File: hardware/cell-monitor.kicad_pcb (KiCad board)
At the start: 2 copper layers, 23 x 45 mm, 15 parts, among them J1 CELL, J2 COMM, J3 COMM, Q1 SI2312BDS, U1 ATTINY85, U2 ADuM1201AR

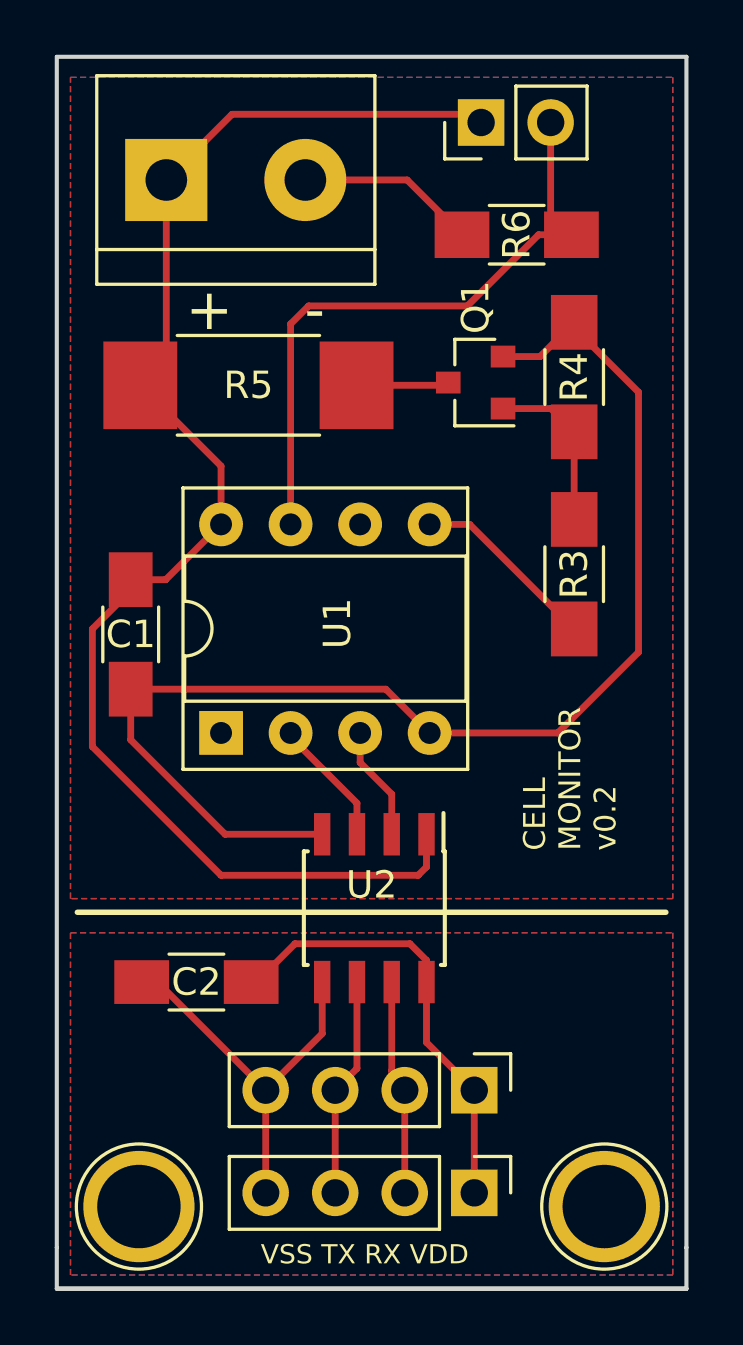
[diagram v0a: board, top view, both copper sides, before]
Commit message: Remove temp related hardware
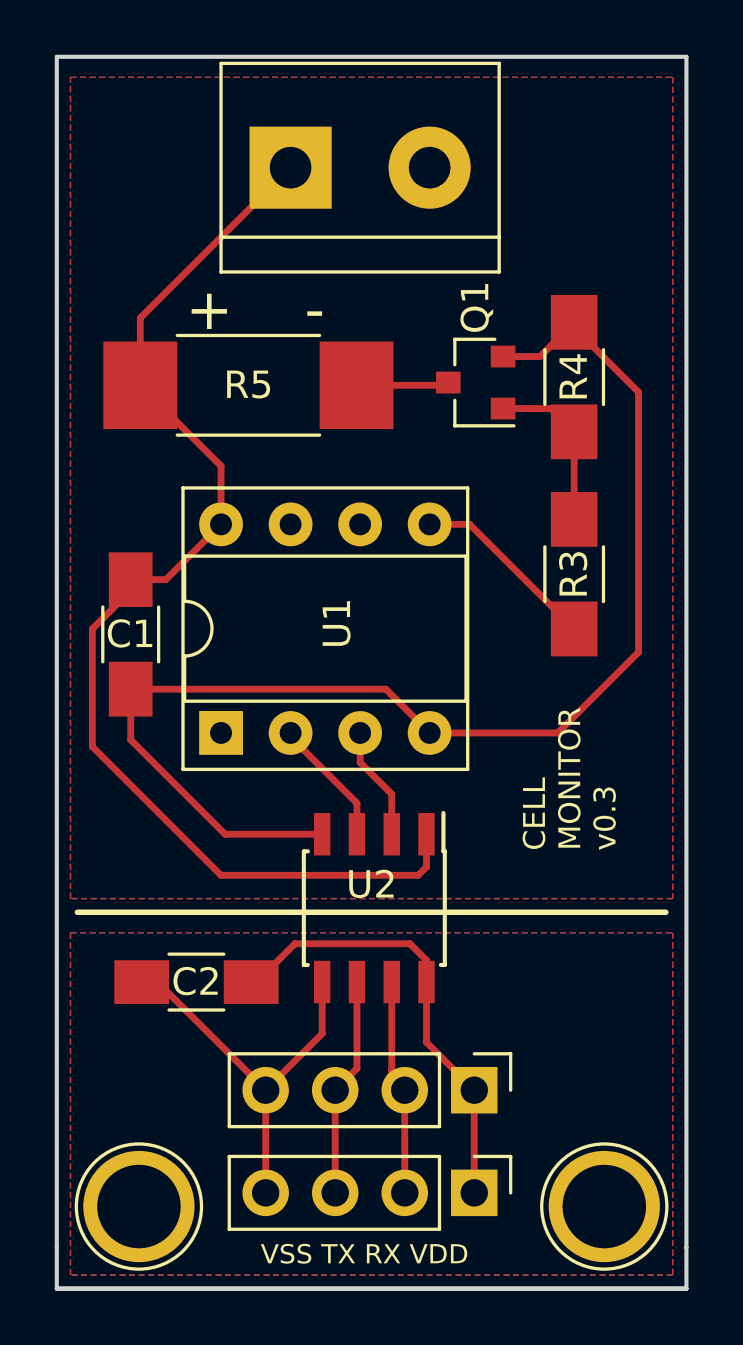
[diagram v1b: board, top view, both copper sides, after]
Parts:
- removed R6: 100k, Resistors_SMD:R_1206_HandSoldering
- removed TH1: 100k, Pin_Headers:Pin_Header_Straight_1x02_Pitch2.54mm
- moved J1 4.56 mm to (78.5, 62.5)
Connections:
- U1 pad 1: Net-(U1-Pad1) -> unconnected-(U1-PB5-Pad1)
- U1 pad 6: Net-(U1-Pad6) -> unconnected-(U1-PB1-Pad6)
- U1 pad 7: /P2 -> unconnected-(U1-PB2-Pad7)
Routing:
- net /P2: track 23.3 -> 0.00 mm
- net VCC: track 56.8 -> 44.2 mm
- net GND: track 53.4 -> 46.8 mm
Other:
- net class Default removed
- board text added: "CELL MONITOR v0.3"
- board text removed: "CELL MONITOR v0.2"
